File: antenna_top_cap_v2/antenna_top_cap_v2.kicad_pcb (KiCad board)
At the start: 4 copper layers, 100 x 100 mm, 70 parts, among them IC1 PCT2075DP,118, J1 Battery Charge Bypass, J10 USB_B_Micro_FC, J11 USB_B_Micro_EPS, J12 FC Board Connector, J13 USB_B_Micro, J14 BM04B-SRSS-TB(LF)(SN), J15 USB_B_Micro, J16 BM04B-SRSS-TB(LF)(SN), J17 BM04B-SRSS-TB(LF)(SN)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

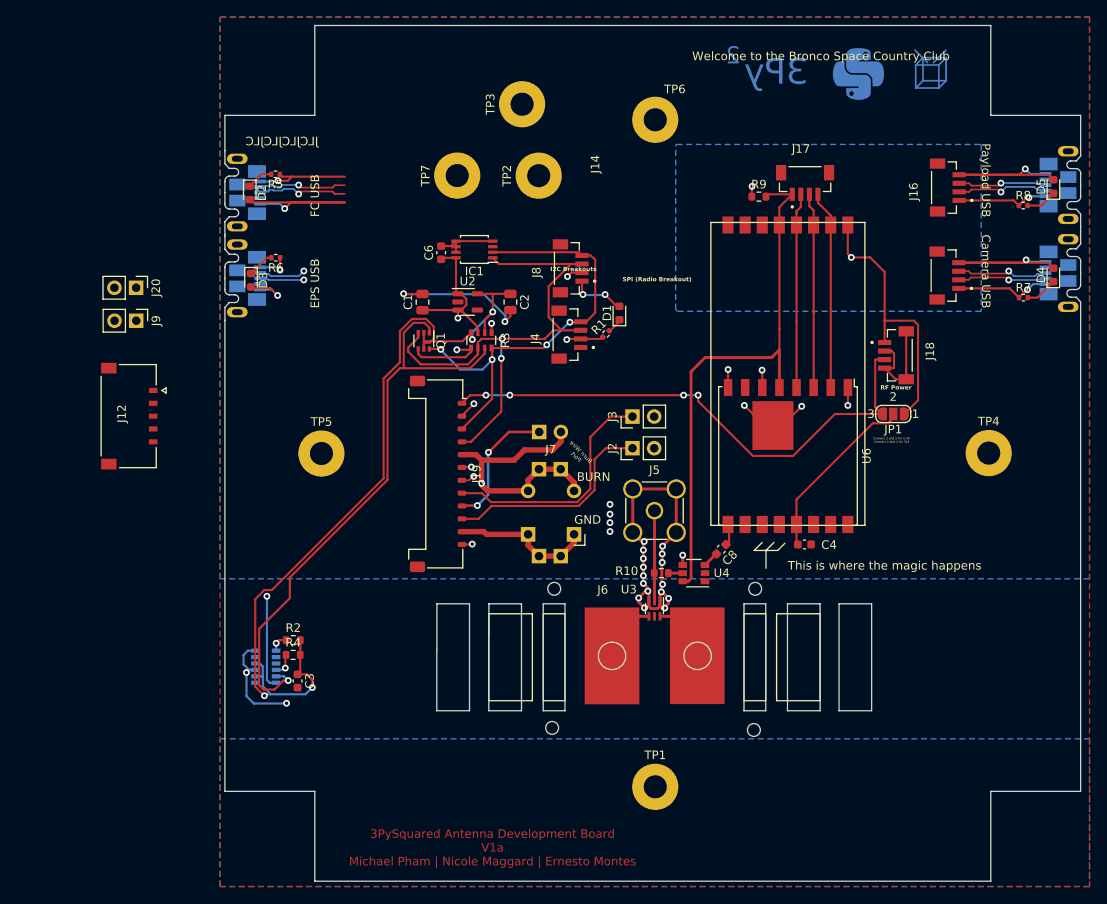
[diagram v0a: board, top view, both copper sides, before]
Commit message: Removed J8 (I2C Breakout)
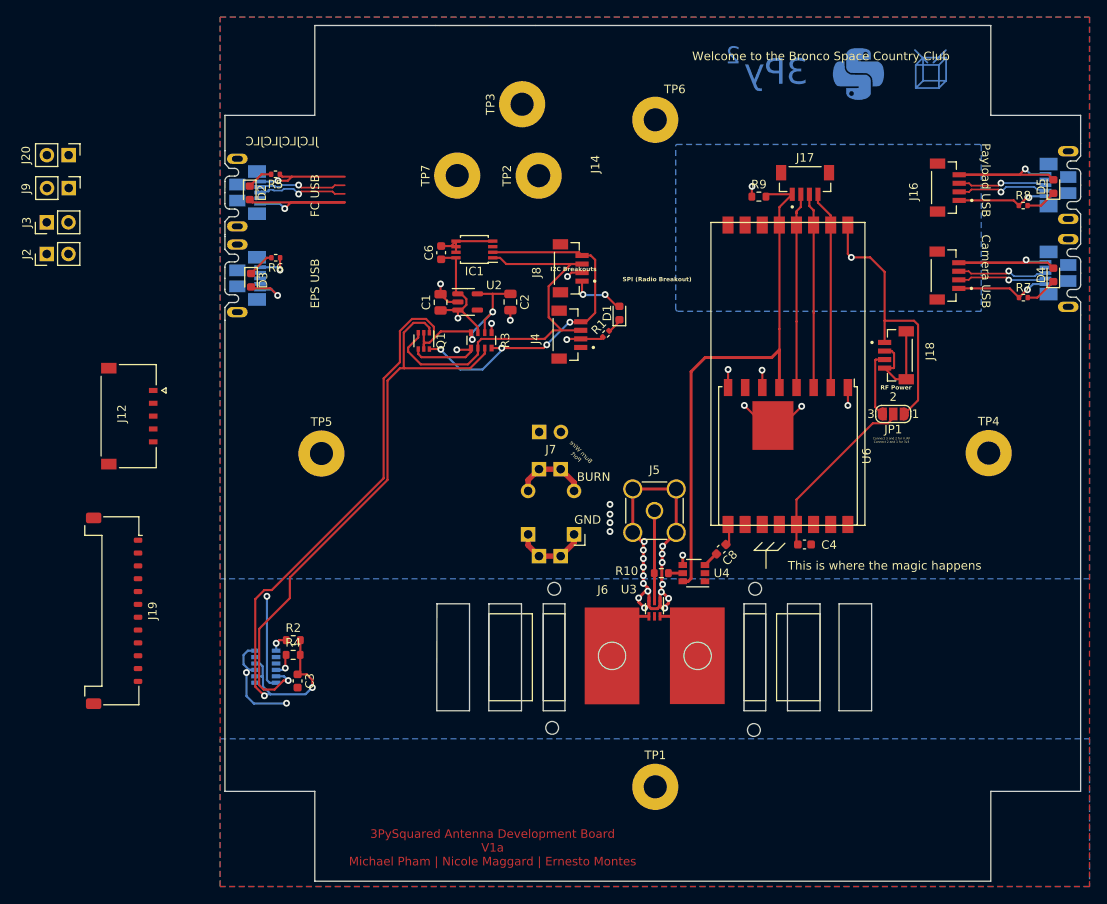
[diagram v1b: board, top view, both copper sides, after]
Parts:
- U1: value VL6180XV0NR/1 -> VL6180V1NR/1
- moved J2 72.1 mm to (94.7, 88.9)
- moved J3 72.1 mm to (94.7, 85.2)
- moved J19 41.1 mm to (102.6, 130.6)
- moved J20 17.4 mm to (97.3, 77.4)
- moved J9 17.4 mm to (97.3, 81.2)
- moved C1 2.11 mm to (140.7, 94.6)
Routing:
- net V_RF: track 62.6 -> 7.75 mm, vias 4 -> 0
- net EPS_USB_D-: track 39.7 -> 0.00 mm, vias 2 -> 0
- net EPS_USB_D+: track 36.6 -> 0.00 mm, vias 2 -> 0
- net GND: track 217.5 -> 181.1 mm, vias 36 -> 34
- net ~{EPS_RESET}: track 28.1 -> 0.00 mm
- net EPS_USBBOOT: track 25.4 -> 0.00 mm
- net Dir_Chrg_In: track 15.5 -> 0.00 mm, vias 2 -> 0
- net SDA1: track 62.1 -> 47.4 mm, vias 2 -> 0
- net SCL1: track 52.0 -> 43.0 mm
- net BURN: track 16.7 -> 8.79 mm
- net +3V3: track 63.9 -> 59.8 mm, vias 9 -> 8
- net 2.8V: track 99.1 -> 97.9 mm

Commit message: fixed the schematic
cool beans
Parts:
- U1: value VL6180V1NR/1 -> VL6180XV0NR/1
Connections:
- net SDA_3V renamed /SDA_3V
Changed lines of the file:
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@@
 	(net 70 "FC_USBBOOT")
 	(net 71 "SDA1")
-	(net 72 "SDA_3V")
+	(net 72 "/SDA_3V")
 	(footprint "Resistor_SMD:R_0603_1608Metric"
 		(layer "F.Cu")
@@
 			(size 0.65 0.4)
 			(layers "F.Cu" "F.Paste" "F.Mask")
-			(net 72 "SDA_3V")
+			(net 72 "/SDA_3V")
 			(pinfunction "S")
 			(pintype "bidirectional")
@@
 			(size 0.8 0.5)
 			(layers "F.Cu" "F.Paste" "F.Mask")
-			(net 72 "SDA_3V")
+			(net 72 "/SDA_3V")
 			(pinfunction "2")
 			(pintype "passive")
@@
 			)
 		)
-		(property "Value" "VL6180V1NR/1"
+		(property "Value" "VL6180XV0NR/1"
 			(at -1.441 -3.066 0)
 			(layer "B.SilkS")
@@
 			(size 0.5 1)
 			(layers "B.Cu" "B.Paste" "B.Mask")
-			(net 72 "SDA_3V")
+			(net 72 "/SDA_3V")
 			(pinfunction "SDA")
 			(pintype "bidirectional")
